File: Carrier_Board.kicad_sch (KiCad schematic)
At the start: 6 parts

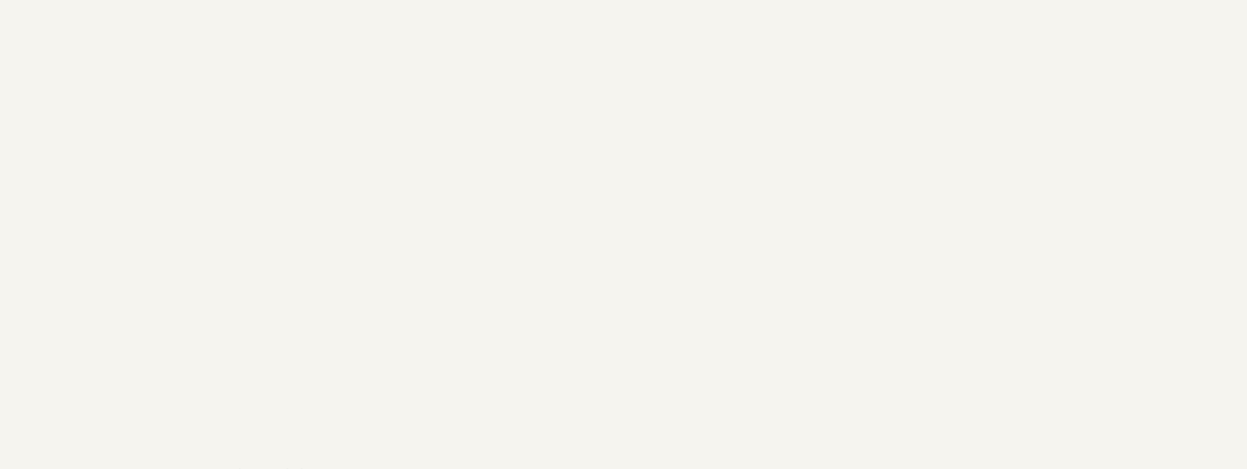
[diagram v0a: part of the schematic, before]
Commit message: Created new Heiarchal sheet for audio, and started to arrange passive components for the HDMI connector
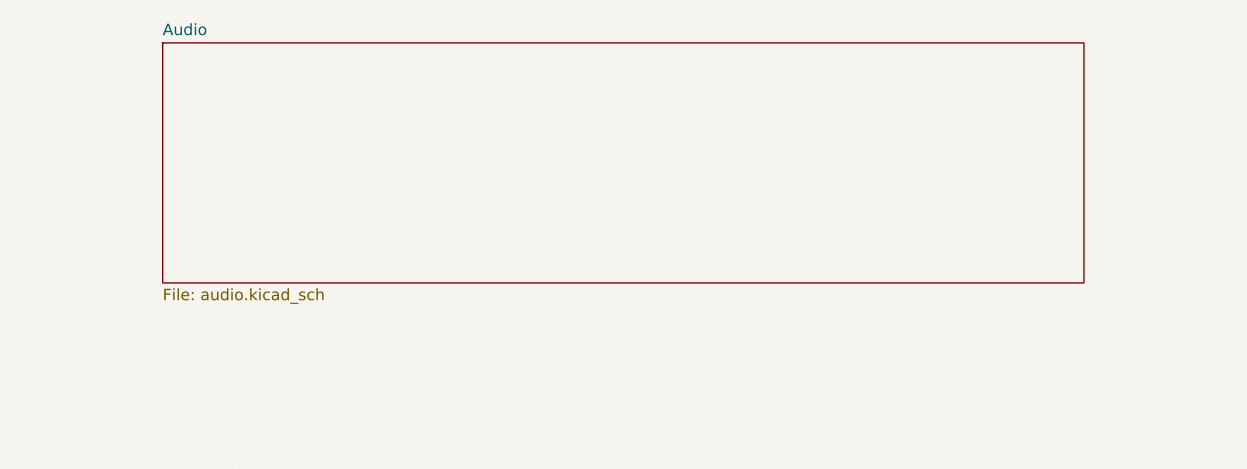
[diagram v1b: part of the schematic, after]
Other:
- added sheet Audio (audio.kicad_sch)
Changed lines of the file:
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@@
+	)
+	(sheet
+		(at 203.2 26.67)
+		(size 102.362 26.67)
+		(exclude_from_sim no)
+		(in_bom yes)
+		(on_board yes)
+		(dnp no)
+		(fields_autoplaced yes)
+		(stroke
+			(width 0.1524)
+			(type solid)
+		)
+		(fill
+			(color 0 0 0 0)
+		)
+		(property "Sheetname" "Audio"
+			(at 203.2 25.9584 0)
+			(show_name no)
+			(do_not_autoplace no)
+			(effects
+				(font
+					(size 1.27 1.27)
+				)
+				(justify left bottom)
+			)
+		)
+		(property "Sheetfile" "audio.kicad_sch"
+			(at 203.2 53.9246 0)
+			(show_name no)
+			(do_not_autoplace no)
+			(effects
+				(font
+					(size 1.27 1.27)
+				)
+				(justify left top)
+			)
+		)
+		(instances
+			(project "Carrier_Board"
+				(path "/e768274e-12f3-4f83-96f6-abb7638e0bc1"
+					(page "11")
+				)
+			)
+		)
 	)
 	(sheet

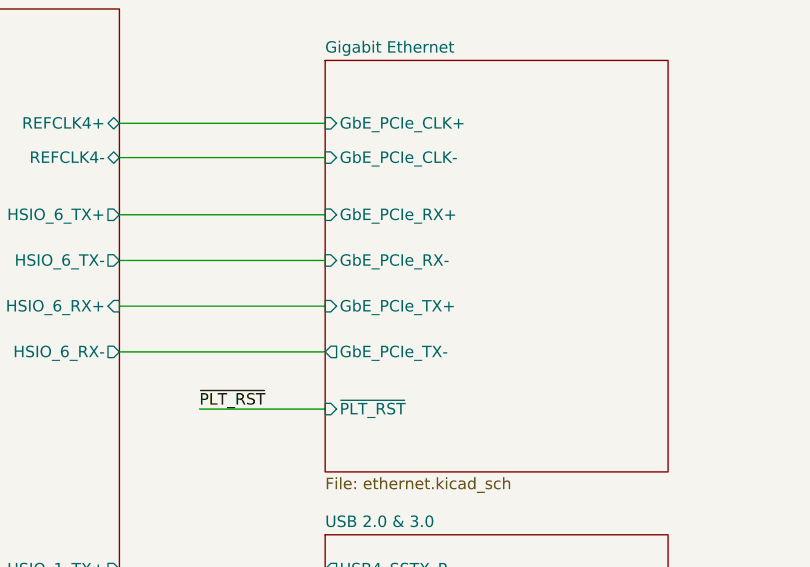
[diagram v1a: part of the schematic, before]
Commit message: Found and fixed a routing mismatch in the gigabit RX TX pin mis assignment
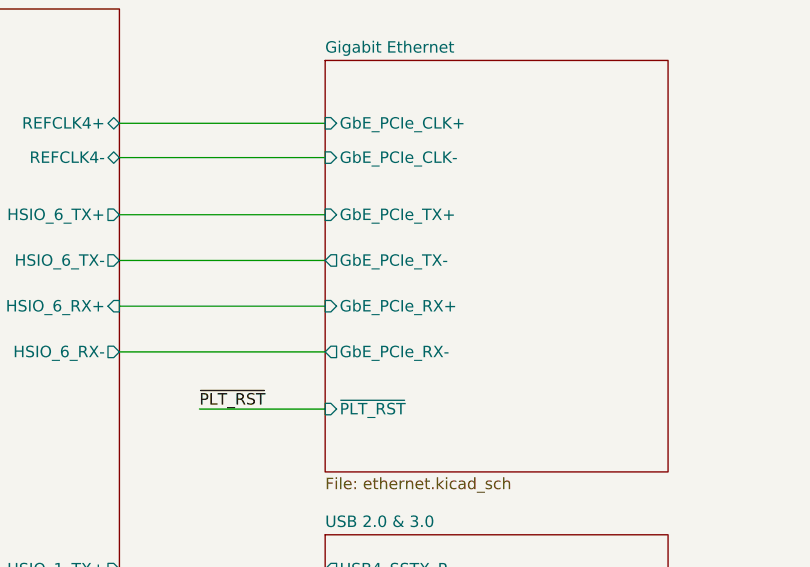
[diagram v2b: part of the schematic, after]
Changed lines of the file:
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@@
 			)
 		)
-		(pin "GbE_PCIe_RX+" input
+		(pin "GbE_PCIe_TX+" input
 			(at 325.12 99.06 180)
 			(effects
@@
 			)
 		)
-		(pin "GbE_PCIe_RX-" input
+		(pin "GbE_PCIe_TX-" output
 			(at 325.12 104.14 180)
 			(effects
@@
 			)
 		)
-		(pin "GbE_PCIe_TX+" input
+		(pin "GbE_PCIe_RX+" input
 			(at 325.12 109.22 180)
 			(effects
@@
 			)
 		)
-		(pin "GbE_PCIe_TX-" output
+		(pin "GbE_PCIe_RX-" output
 			(at 325.12 114.3 180)
 			(effects

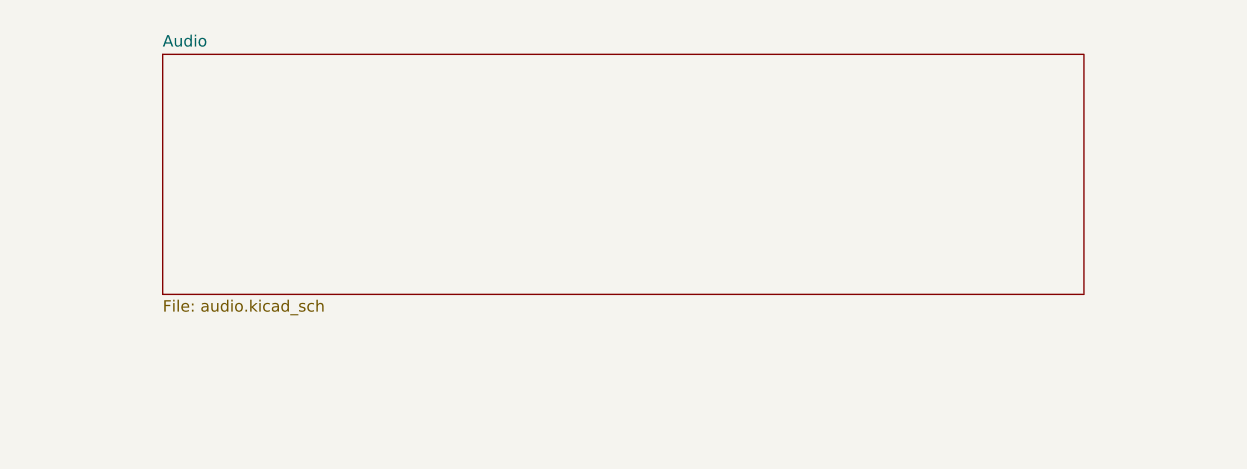
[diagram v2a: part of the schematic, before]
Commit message: Freed up some panda module labels for the wifi/bluetooth chip, and also organized the routes for the gpio connectors into blue layer 2 bundals... not fully connected yet
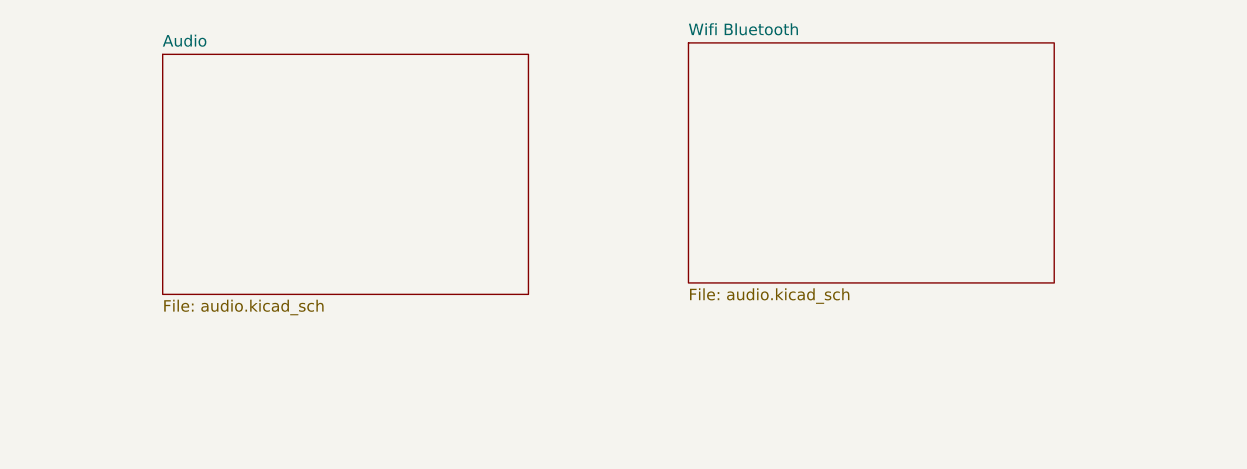
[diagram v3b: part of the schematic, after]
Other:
- added sheet Wifi Bluetooth (audio.kicad_sch)
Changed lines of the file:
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@@
 	(sheet
 		(at 203.2 26.67)
-		(size 102.362 26.67)
+		(size 40.64 26.67)
 		(exclude_from_sim no)
 		(in_bom yes)
@@
 				)
 			)
+		)
+	)
+	(sheet
+		(at 261.62 25.4)
+		(size 40.64 26.67)
+		(exclude_from_sim no)
+		(in_bom yes)
+		(on_board yes)
+		(dnp no)
+		(fields_autoplaced yes)
+		(stroke
+			(width 0.1524)
+			(type solid)
+		)
+		(fill
+			(color 0 0 0 0)
+		)
+		(property "Sheetname" "Wifi Bluetooth"
+			(at 261.62 24.6884 0)
+			(show_name no)
+			(do_not_autoplace no)
+			(effects
+				(font
+					(size 1.27 1.27)
+				)
+				(justify left bottom)
+			)
+		)
+		(property "Sheetfile" "audio.kicad_sch"
+			(at 261.62 52.6546 0)
+			(show_name no)
+			(do_not_autoplace no)
+			(effects
+				(font
+					(size 1.27 1.27)
+				)
+				(justify left top)
+			)
+		)
+		(instances
+			(project "Carrier_Board"
+				(path "/e768274e-12f3-4f83-96f6-abb7638e0bc1"
+					(page "12")
+				)
+			)
